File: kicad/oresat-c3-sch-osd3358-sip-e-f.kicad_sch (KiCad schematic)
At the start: 5 parts, among them U1 OSD3358-512M-BSM

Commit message: BOM cleanups; modified test points to not show up on BOMs, fixed some minor BOM shenaigans (3k vs 3.0k), and imported into the board.
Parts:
- TP19, TP20, TP21, TP22: now left out of the parts list
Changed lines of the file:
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@@
 		(at 187.96 162.56 0)
 		(unit 1)
-		(exclude_from_sim no)
-		(in_bom yes)
+		(exclude_from_sim yes)
+		(in_bom no)
 		(on_board yes)
 		(dnp no)
@@
 			)
 		)
-		(property "Description" ""
+		(property "Description" "1mm round SMT test point"
 			(at 187.96 162.56 0)
 			(effects
@@
 		(at 187.96 167.64 0)
 		(unit 1)
-		(exclude_from_sim no)
-		(in_bom yes)
+		(exclude_from_sim yes)
+		(in_bom no)
 		(on_board yes)
 		(dnp no)
@@
 			)
 		)
-		(property "Description" ""
+		(property "Description" "1mm round SMT test point"
 			(at 187.96 167.64 0)
 			(effects
@@
 		(at 187.96 177.8 0)
 		(unit 1)
-		(exclude_from_sim no)
-		(in_bom yes)
+		(exclude_from_sim yes)
+		(in_bom no)
 		(on_board yes)
 		(dnp no)
@@
 			)
 		)
-		(property "Description" ""
+		(property "Description" "1mm round SMT test point"
 			(at 187.96 177.8 0)
 			(effects
@@
 		(at 187.96 172.72 0)
 		(unit 1)
-		(exclude_from_sim no)
-		(in_bom yes)
+		(exclude_from_sim yes)
+		(in_bom no)
 		(on_board yes)
 		(dnp no)
@@
 			)
 		)
-		(property "Description" ""
+		(property "Description" "1mm round SMT test point"
 			(at 187.96 172.72 0)
 			(effects

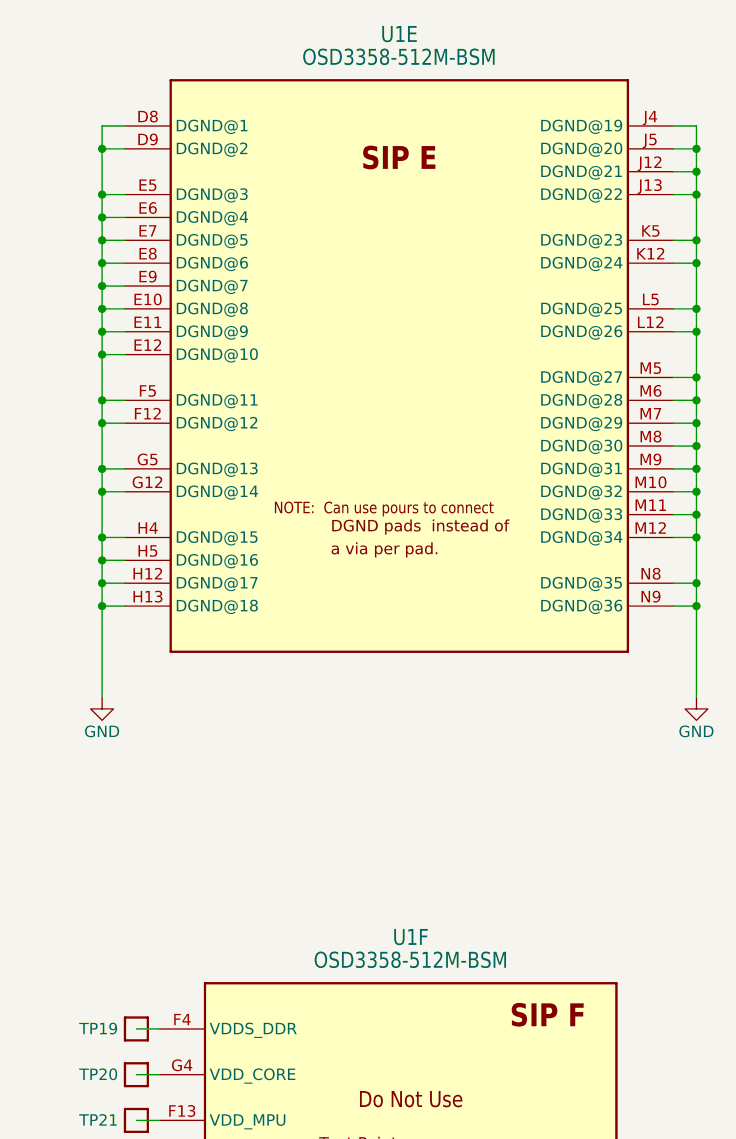
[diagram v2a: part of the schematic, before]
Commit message: Fixed more part numbers while in process of doing BOM inventory, including eMMC and FRAM.
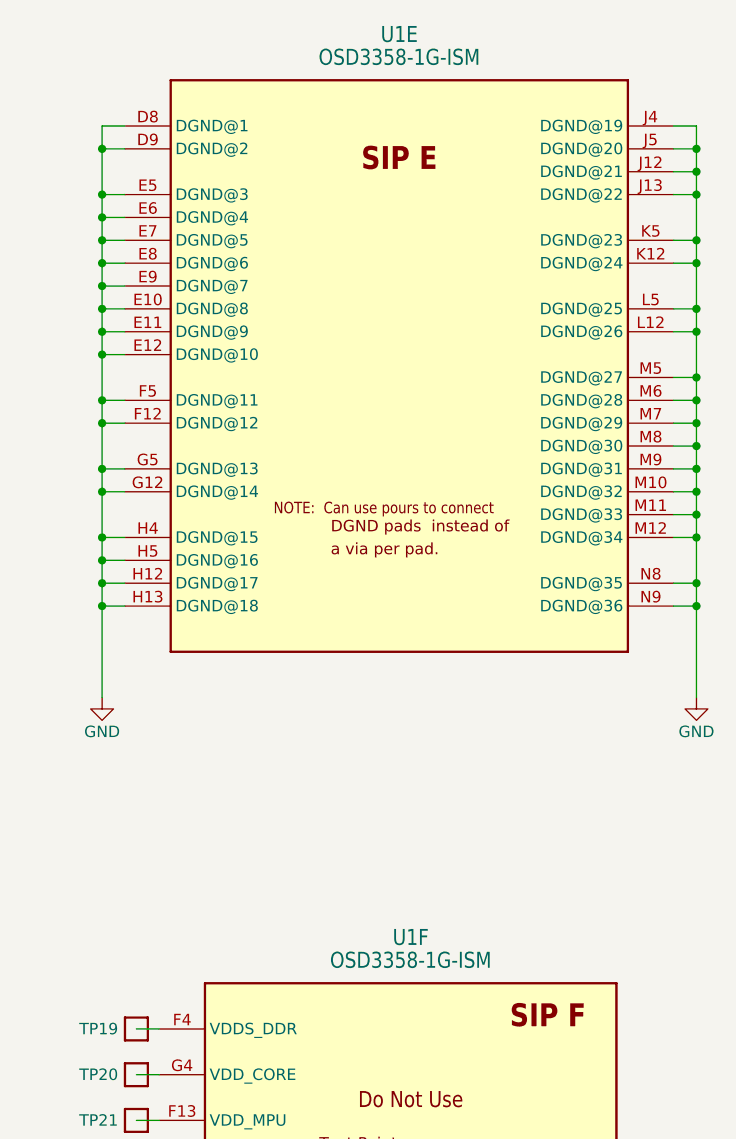
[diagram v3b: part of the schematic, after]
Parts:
- U1: value OSD3358-512M-BSM -> OSD3358-1G-ISM
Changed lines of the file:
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@@
 			)
 		)
-		(property "Value" "OSD3358-512M-BSM"
+		(property "Value" "OSD3358-1G-ISM"
 			(at 218.44 154.94 0)
 			(effects
@@
 			)
 		)
-		(property "Value" "OSD3358-512M-BSM"
+		(property "Value" "OSD3358-1G-ISM"
 			(at 217.17 54.61 0)
 			(effects

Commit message: Added MFR, MPN, Description, DST, and DPN to all components using the amazing KiCAD table properties editor. Yay KiCAD. Attemping to make the BOM be self-assembling.
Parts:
- U1: DPN (none) -> 1676-OSD3358-1G-ISM-ND; DST (none) -> Digi-Key; Distributor DigiKey -> (none); MFR (none) -> Octavo Systems; MPN OSD3358-512M-BSM -> OSD3358-1G-ISM
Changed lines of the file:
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@@
 			)
 		)
-		(property "Description" "OSD335x Embedded Module 1GHz 512MB"
+		(property "Description" "Embedded Module ARM® Cortex®-A8, AM3358 1GHz 1GB"
 			(at 218.44 78.74 0)
 			(effects
@@
 			)
 		)
-		(property "Distributor" "DigiKey"
-			(at 218.44 81.28 0)
-			(effects
-				(font
-					(size 1.27 1.27)
-				)
-				(hide yes)
-			)
-		)
-		(property "MPN" "OSD3358-512M-BSM"
+		(property "MPN" "OSD3358-1G-ISM"
 			(at 218.44 83.82 0)
+			(effects
+				(font
+					(size 1.27 1.27)
+				)
+				(hide yes)
+			)
+		)
+		(property "DPN" "1676-OSD3358-1G-ISM-ND"
+			(at 218.44 182.88 0)
+			(effects
+				(font
+					(size 1.27 1.27)
+				)
+				(hide yes)
+			)
+		)
+		(property "DST" "Digi-Key"
+			(at 218.44 182.88 0)
+			(effects
+				(font
+					(size 1.27 1.27)
+				)
+				(hide yes)
+			)
+		)
+		(property "MFR" "Octavo Systems"
+			(at 218.44 182.88 0)
 			(effects
 				(font
@@
 			)
 		)
-		(property "Description" "OSD335x Embedded Module 1GHz 512MB"
+		(property "Description" "Embedded Module ARM® Cortex®-A8, AM3358 1GHz 1GB"
 			(at 217.17 -16.51 0)
 			(effects
@@
 			)
 		)
-		(property "Distributor" "DigiKey"
-			(at 217.17 -13.97 0)
-			(effects
-				(font
-					(size 1.27 1.27)
-				)
-				(hide yes)
-			)
-		)
-		(property "MPN" "OSD3358-512M-BSM"
+		(property "MPN" "OSD3358-1G-ISM"
 			(at 217.17 -11.43 0)
 			(effects
 				(font
+					(size 1.27 1.27)
+				)
+				(hide yes)
+			)
+		)
+		(property "DPN" "1676-OSD3358-1G-ISM-ND"
+			(at 217.17 87.63 0)
+			(effects
+				(font
+					(size 1.27 1.27)
+				)
+				(hide yes)
+			)
+		)
+		(property "DST" "Digi-Key"
+			(at 217.17 87.63 0)
+			(effects
+				(font
+					(size 1.27 1.27)
+				)
+				(hide yes)
+			)
+		)
+		(property "MFR" "Octavo Systems"
+			(at 217.17 87.63 0)
+			(effects
+				(font

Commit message: C3 v6.1 release
Updated to KiCad 9.0.6. Updated to version 6.1; there are small changes that have been lost in time. Lots of new ERC and DRC errors that need to be cleaned up.
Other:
- company: (none) -> Portland State Aerospace Society
- title: OreSat C3: OSD3358 SIP E + F -> OreSat C3 Card
